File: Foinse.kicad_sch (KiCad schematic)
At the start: 154 parts, among them J1 Conn_ARM_JTAG_SWD_10, J10 Conn_02x03_Odd_Even, J2 2060-1452, J3 ESQ-110-14-G-D, J4 PJ-002AH, J5 2060-1452/998-404, J8 2601-1108, J9 USB_C_Receptacle_USB2.0_16P, Q1 AO3400A, Q10 AO3400A, Q11 AO3400A, Q12 AO3400A, Q13 AO3400A, Q14 AO3400A, Q2 AO3400A, Q3 AO3400A, Q4 AO3400A, Q5 AO3400A, Q6 AO3400A, Q7 AO3400A, Q8 AO3400A, Q9 AO3400A, U1 STM32F072C8Tx, U10 LTV-817, U11 LTV-817, U12 LTV-817, U13 LTV-817, U14 USBLC6-2SC6, U15 INA239AIDGSR, U16 INA239AIDGSR, U17 LTC4412xS6, U18 LTV-817, U19 TPS56A37RPAR, U2 TLV70433DBVT, U3 LTV-817, U4 TJA1051T-3, U5 TPS563203, U7 LTV-817, U8 LTV-817, U9 LTV-817

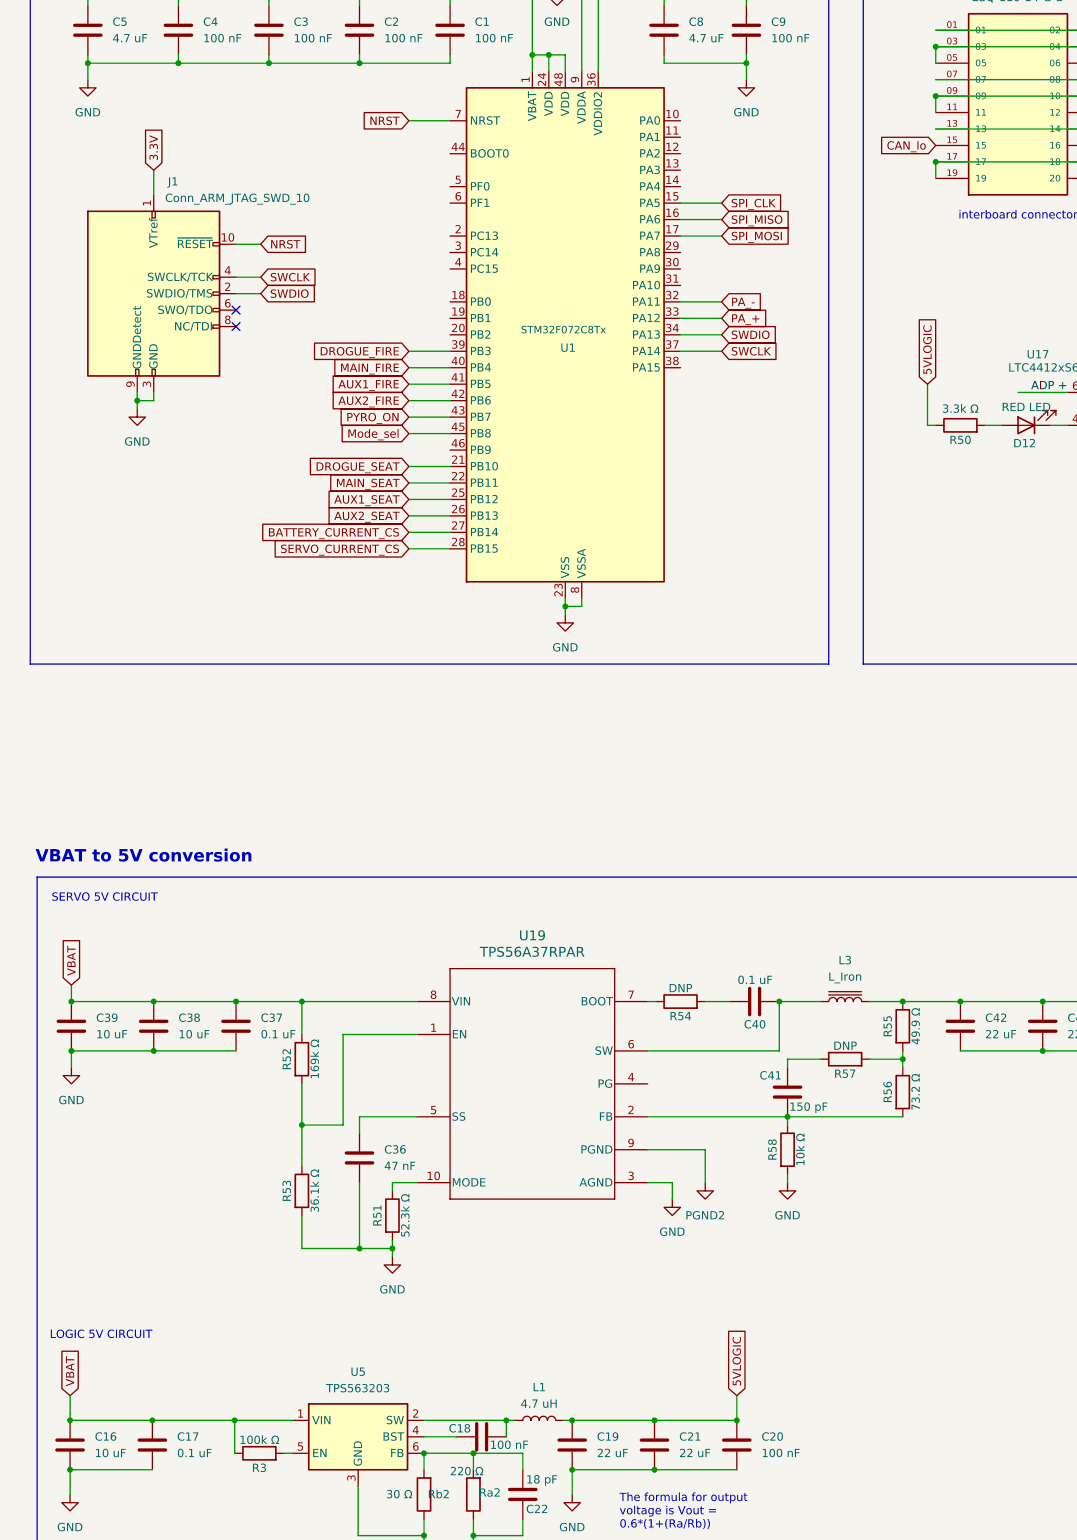
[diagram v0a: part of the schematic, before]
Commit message: Assighned all footprints
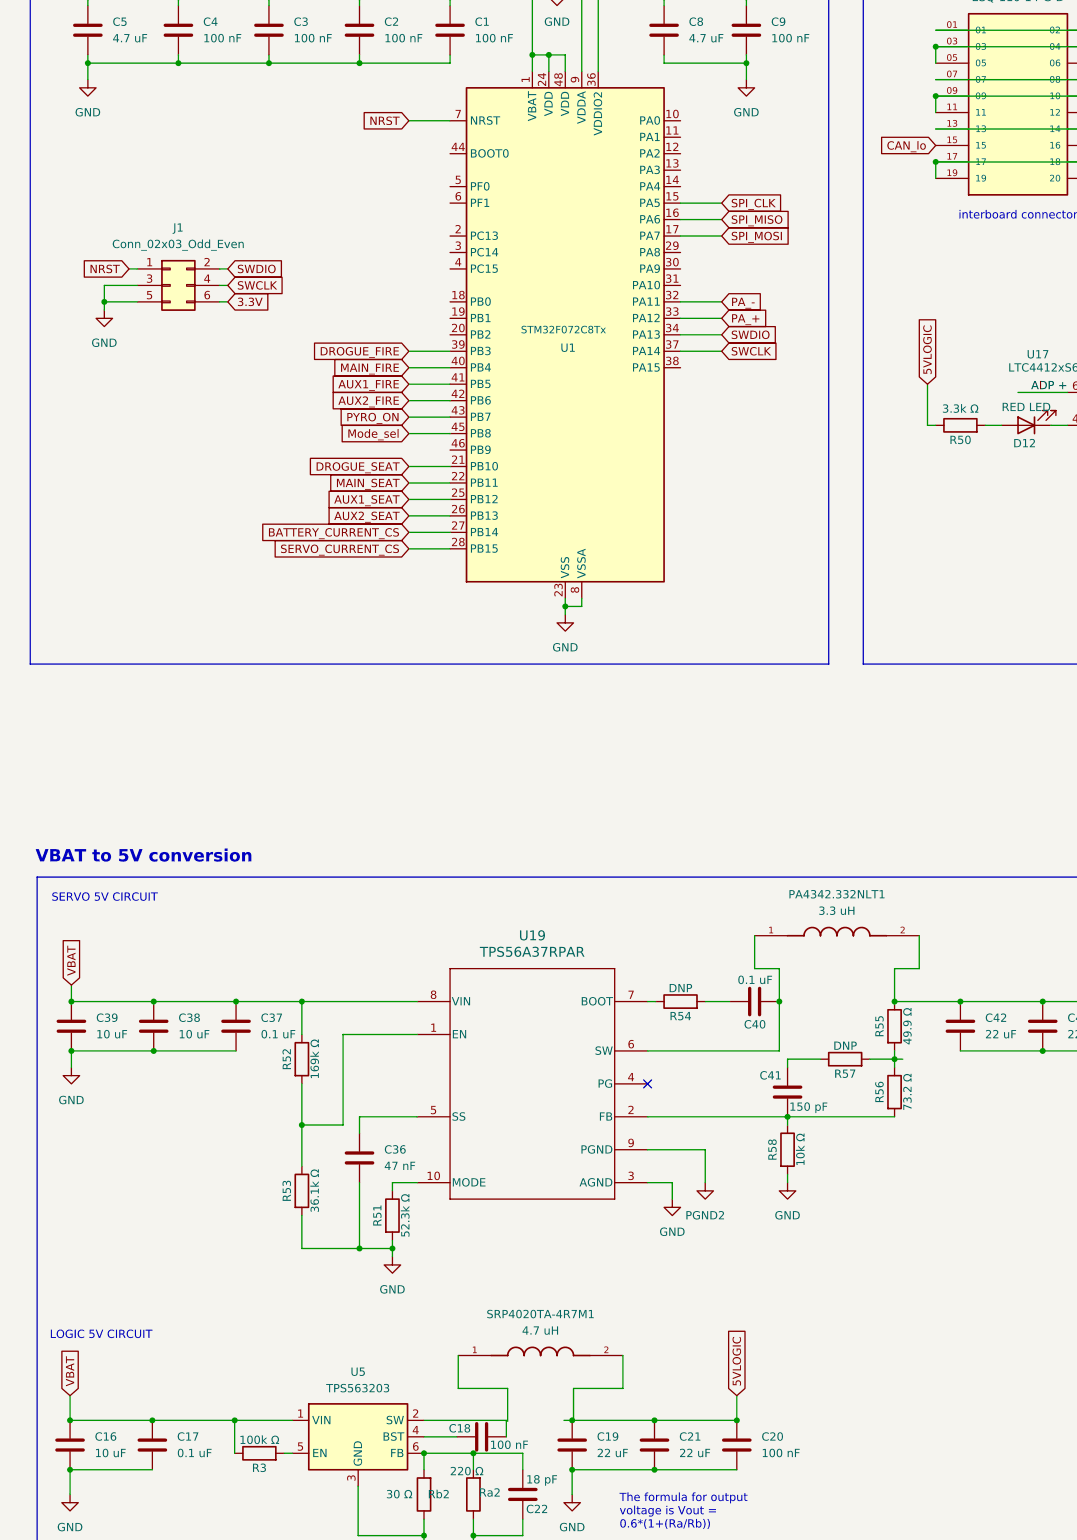
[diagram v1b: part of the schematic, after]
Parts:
- removed J1: Conn_ARM_JTAG_SWD_10, Connector_PinHeader_1.27mm:PinHeader_2x05_P1.27mm_Vertical, symbol Connector:Conn_ARM_JTAG_SWD_10
- removed L1: 4.7 uH, symbol Device:L
- removed L3: L_Iron, symbol Device:L_Iron
- added J1: Conn_02x03_Odd_Even, Connector_PinHeader_1.00mm:PinHeader_2x03_P1.00mm_Vertical, symbol Connector_Generic:Conn_02x03_Odd_Even
- added PA4342.332NLT1: 3.3 uH, Foinse Footprints:IND_PA4342.332NLT, symbol PA4342.332NLT:PA4342.332NLT
- added SRP4020TA-4R7M1: 4.7 uH, Foinse Footprints:IND_SRP4020TA-4R7M, symbol SRP4020TA-4R7M:SRP4020TA-4R7M
- D14: footprint (none) -> Package_TO_SOT_THT:TO-220-3_Vertical
- J2, J5: footprint footprints:WAG -> Foinse Footprints:WAG
- U2: footprint TLV70433DBVT:DBV0005A_N -> Foinse Footprints:DBV0005A_N
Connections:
- net 3.3V: now also J1.6 (Pin_6)
- net 5VSERVO_BS: now also PA4342.332NLT1.2
- net GND: now also J1.3 (Pin_3), J1.5 (Pin_5)
- net NRST: now also J1.1 (Pin_1)
- net SWCLK: now also J1.4 (Pin_4)
- net SWDIO: now also J1.2 (Pin_2)
- net at C40.2, U19.6 (SW): now also PA4342.332NLT1.1
- no-connect marks 7 -> 6
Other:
- moved on the sheet: R55, R56

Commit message: Fixed shit
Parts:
- removed R17, R26, R35, R7: 1-3Ω, Resistor_SMD:R_0402_1005Metric, symbol Device:R
- R10, R30, R39: value 2 Ω -> 2 kΩ
- R11, R40: value 4.7 Ω -> 4.7 kΩ
- R20: value 6 Ω -> 6k Ω
- R21: value 2 Ω -> 2k Ω
- R22, R31: value 4.7 Ω -> 4.7k Ω
- R29, R38, R9: value 6 Ω -> 6 kΩ
- U10, U11, U12, U13, U18, U3, U7, U8, U9: footprint Package_DIP:DIP-4_W7.62mm -> Foinse Footprints:SO4_TOS
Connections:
- net Aux1 neg: now also Q7.3 (D)
- net Aux2 neg: now also Q10.3 (D)
- net Drogue neg: now also Q1.3 (D)
- net GND: now also R12.1, R14.1, R23.1, R32.1, U10.2, U12.2, U18.2, U3.2, U8.2
- net Main neg: now also Q4.3 (D)
- net PGND: no longer R12.1, R14.1, R23.1, R32.1, U10.2, U12.2, U18.2, U3.2, U8.2
- net at Q10.1 (G), Q11.1 (G), R34.1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: no longer Q10.3 (D)
- net at Q1.1 (G), Q2.1 (G), R6.1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: no longer Q1.3 (D)
- net at Q4.1 (G), Q5.1 (G), R16.1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: no longer Q4.3 (D)
- net at Q7.1 (G), Q8.1 (G), R25.1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: no longer Q7.3 (D)
